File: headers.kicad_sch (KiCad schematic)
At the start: 1 part, among them J13 SWD Header

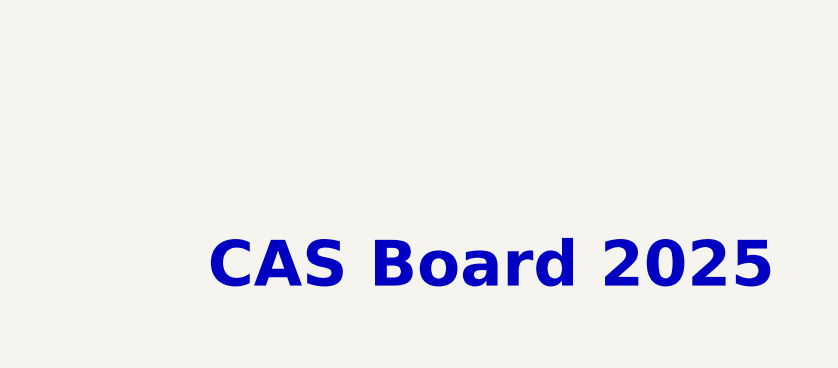
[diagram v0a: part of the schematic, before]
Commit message: remove camera power and interface headers and pins from schematic and PCB
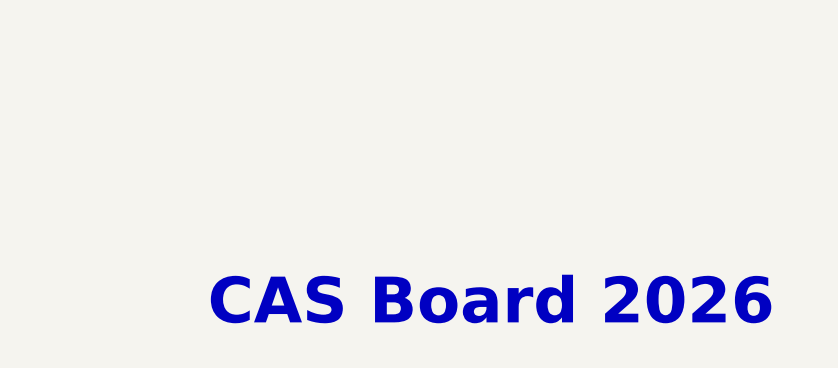
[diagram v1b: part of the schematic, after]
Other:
- note added: "CAS Board 2026"
- note removed: "CAS Board 2025"
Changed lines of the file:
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@@
 	(generator_version "9.0")
 	(paper "A4")
-	(text "CAS Board 2025\n\n"
+	(text "CAS Board 2026"
 		(exclude_from_sim no)
 		(at 209.55 177.8 0)
